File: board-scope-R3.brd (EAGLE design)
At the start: 80 x 55 mm, 71 parts, among them IC3 STM32F103C8T, J2 632723300011, U1 HD3SS3220IRNHT, U2 TUSB8020B, U3 FT600Q-T, U4 ICE40HX1K-VQ100VQ-100, U5 25F32006WSOI, U7 TPS54386, X1 30Mhz, X2 8Mhz

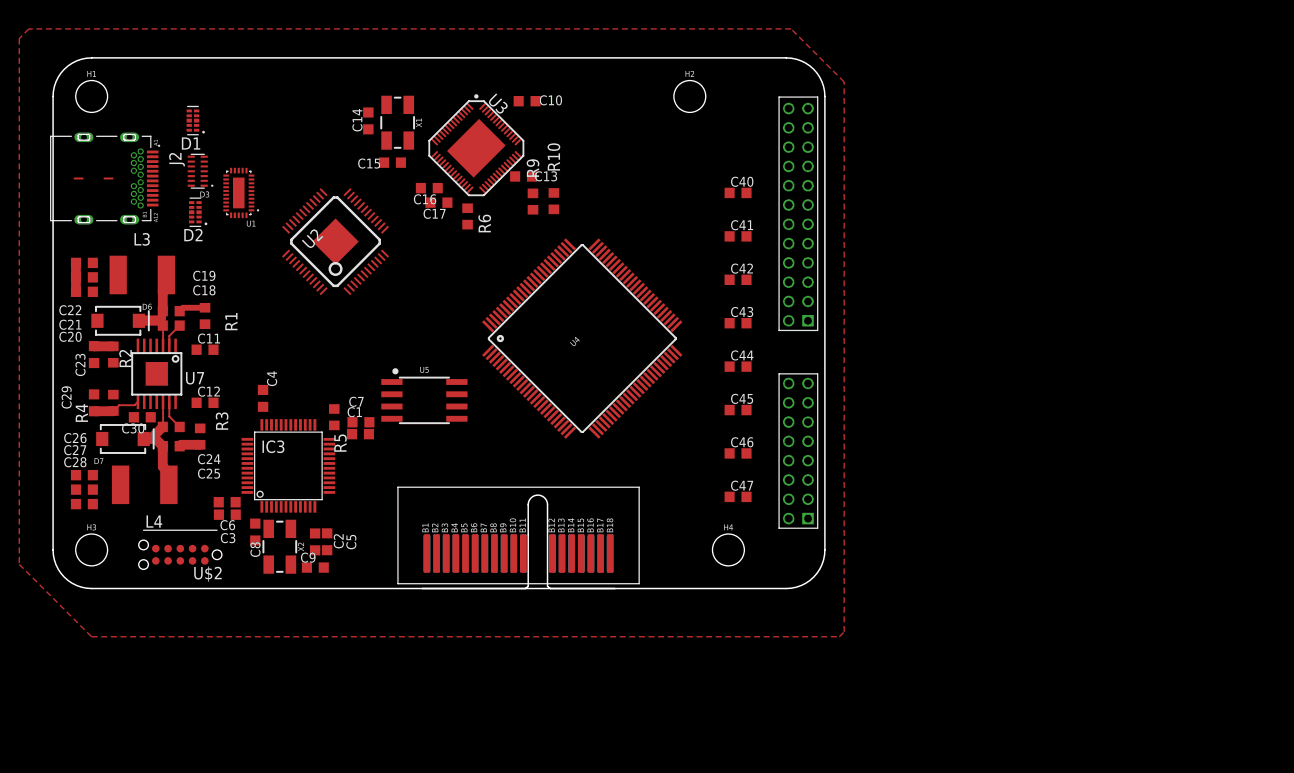
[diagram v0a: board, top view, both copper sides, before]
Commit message: routed power and usb
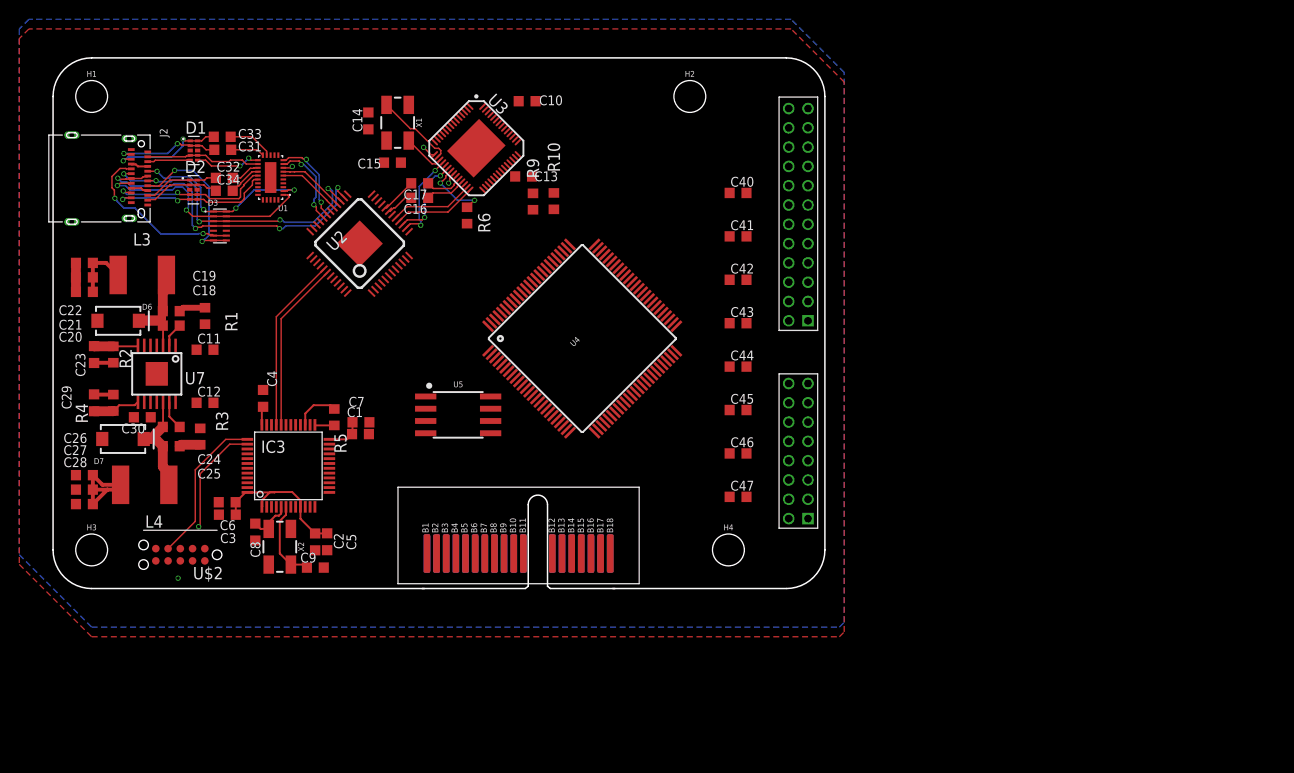
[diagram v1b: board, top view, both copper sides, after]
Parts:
- added C31, C32, C33, C34: 0.47uF, rcl:C0603K
- J2: value 632723300011 -> 12401598E4#2A; device 632723300011:WURTH_632723X00011 -> 12401598E4_2A:AMPHENOL_12401598E4#2A
- moved D3 6.12 mm to (27.3, 47.6), turned to 0 degrees
- moved U5 3.81 mm to (52.0, 28.0)
- moved U1 3.67 mm to (32.5, 52.6)
- moved J2 3.40 mm to (19.1, 52.5)
- moved D1 3.10 mm to (24.6, 55.4), turned to 0 degrees
- moved C17 2.83 mm to (48.0, 52.0)
- moved U2 2.51 mm to (41.8, 45.8)
- moved D2 2.34 mm to (24.6, 51.3), turned to 0 degrees
- moved C16 1.41 mm to (48.0, 50.5)
- moved R6 0.11 mm to (52.9, 48.7)
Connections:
- removed net N$10: J2.S1, J2.S2, J2.S3, J2.S4, J2.S5, J2.S6
- removed net N$11: J2.A1, J2.A12, J2.B1, J2.B12, J2.GND, J2.GND1
- removed net N$12: U1.16
- removed net N$13: U1.17
- removed net N$14: U1.20
- removed net N$15: U1.21
- removed net N$9: J2.A4, J2.A9, J2.B4, J2.B9
- new net SSRXN1_UP_C: C33.2, U1.14
- new net SSRXN2_UP_C: C32.2, U1.18
- new net SSRXP1_UP_C: C31.2, U1.15
- new net SSRXP2_UP_C: C34.2, U1.19
- net GND: now also J2.A1, J2.A12, J2.B1, J2.B12, J2.SH1, J2.SH2, J2.SH3, J2.SH4
- net SSRXN1_UP: now also C33.1, D1.1, D1.10; no longer D1.4, D1.7, U1.14
- net SSRXN2_UP: now also C32.1, D2.1, D2.10; no longer D2.5, D2.6, U1.18
- net SSRXP1_UP: now also C31.1, D1.2, D1.9; no longer D1.5, D1.6, U1.15
- net SSRXP2_UP: now also C34.1, D2.2, D2.9; no longer D2.4, D2.7, U1.19
- net SSTXN1_UP: now also D1.5, D1.6, U1.16; no longer D1.1, D1.10
- net SSTXN2_UP: now also D2.4, D2.7, U1.20; no longer D2.2, D2.9
- net SSTXP1_UP: now also D1.4, D1.7, U1.17; no longer D1.2, D1.9
- net SSTXP2_UP: now also D2.5, D2.6, U1.21; no longer D2.1, D2.10
- net V_USB: now also J2.A4, J2.A9, J2.B4, J2.B9
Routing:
- net DP_UP: track 0.00 -> 34.7 mm, vias 0 -> 4
- net +3V3: track 0.00 -> 34.0 mm, vias 0 -> 3
- net DN_UP: track 0.00 -> 32.2 mm, vias 0 -> 5
- net CC2: track 0.00 -> 23.8 mm, vias 0 -> 2
- net CC1: track 0.00 -> 20.3 mm, vias 0 -> 4
- net BM_DP: track 0.00 -> 18.2 mm
- net SBU2: track 0.00 -> 18.0 mm, vias 0 -> 2
- net BM_TDI: track 0.00 -> 17.9 mm, vias 0 -> 2
- net BM_DM: track 0.00 -> 17.8 mm
- net SSTXN2_UP: track 0.00 -> 16.9 mm, vias 0 -> 2
- net SSTXP2_UP: track 0.00 -> 16.9 mm, vias 0 -> 2
- net SBU1: track 0.00 -> 16.3 mm, vias 0 -> 2
- net BM_TCK: track 0.00 -> 16.0 mm
- net VCCINT: track 0.00 -> 13.5 mm
- net SSTXP1_UP: track 0.00 -> 12.0 mm
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- added copper zone on layer 15, net GND
- added copper zone on layer 16, net GND
- added copper zone on layer 2, net GND
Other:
- outline, holes or cut-outs redrawn

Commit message: saving
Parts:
- removed C44, C45, C46, C47: 0.1uF, rcl:C0603K
- added B10, B11, B12, B13, B14, B15, B8, B9: (no value), SparkFun-LED:LED-0603
- added C600, C610, C620, C650, C651: 1uF, rcl:C0603K
- added C601, C611, C621, C652, C653: 0.1uF, rcl:C0603K
- added C602, C603, C612, C613, C622, C623, C654, C655, C656: 10nF, rcl:C0603K
- added D4: 1A/23V/620mV, SparkFun-DiscreteSemi:SOD-323
- added R11: 330, mylib:CTS743C163
- added R7, R8: 10k, rcl:R0603
- added S1, S3: (no value), mylib:TACTILE_SWITCH_SMD_5.2MM
- C630: value 0.1uF -> 1uF
- C632, C633: value 0.1uF -> 10nF
- U4: value ICE40HX1K-VQ100VQ-100 -> ICE40HX1K-VQ100; device ice40hx1k-vq100:TQFP100 -> mylib:QFP50P1600X1600X120-100N
- moved U5 12.4 mm to (40.9, 33.5)
- moved U4 2.62 mm to (66.3, 38.1), turned to 315 degrees
- moved C2 1.22 mm to (38.4, 14.8)
- moved C5 1.22 mm to (39.6, 14.8)
- moved C9 1.22 mm to (38.4, 12.1)
- moved X2 1.22 mm to (34.7, 14.3)
- moved C8 1.22 mm to (32.2, 15.8)
- renumbered C40 to C630, C41 to C631, C42 to C632, C43 to C633
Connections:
- net VPP_DIRECT_FAST renamed VPP_FAST
- removed net GND$0: U4.5
- removed net GND$1: U4.17
- removed net GND$2: U4.23
- removed net GND$3: U4.32
- removed net GND$4: U4.39
- removed net GND$5: U4.47
- removed net GND$6: U4.55
- removed net GND$8: U4.84
- removed net GND$9: U4.98
- removed net ICE40_VCCIO1: C44.1, C45.1, C46.1, C47.1
- removed net IOT_78: U4.82
- removed net VCC: U4.11, U5.8
- removed net VCCIO_0$1: U4.92
- removed net VCCIO_2: U4.31, U4.38
- removed net VCCIO_3: U4.6
- removed net VCCIO_3$: U4.14
- removed net VCCIO_3$1: U4.22
- removed net VCC_IO_1: U4.58
- removed net VCC_IO_1$1: U4.67
- removed net VDD_SPI_IO: U4.50
- removed net VPP_2V5_PUMP: U4.75
- new net BM_MISO: IC3.40, U4.46, U5.2
- new net BM_MOSI: IC3.41, U4.45, U5.5
- new net BM_SCK: IC3.39, U4.48, U5.6
- new net BTN_A: S1.3
- new net BTN_B: S3.3
- new net ICE_CDONE: IC3.42
- new net ICE_CRESET: IC3.43
- new net ICE_SS: IC3.45, U4.49, U5.1
- new net LED0: R11.9
- new net LED1: R11.10
- new net LED2: R11.11
- new net LED3: R11.12
- new net LED4: R11.13
- new net LED5: R11.14
- new net LED6: R11.15
- new net LED7: R11.16
- new net N$1: D4.C, U4.75
- new net N$13: B8.A, R11.1
- new net N$14: B9.A, R11.2
- new net N$15: B10.A, R11.3
- new net N$2: IC3.46
- new net N$20: B11.A, R11.4
- new net N$21: B12.A, R11.5
- new net N$3: IC3.44, R8.2
- new net N$34: B13.A, R11.6
- new net N$35: B14.A, R11.7
- new net N$36: B15.A, R11.8
- net +3V3: now also D4.A, R7.2, U4.14, U4.22, U4.31, U4.38, U4.50, U4.58, U4.6, U4.67, U4.88, U4.92, U5.8
- net BM_RST: now also R7.1
- net BM_TDO: no longer IC3.39
- net GND: now also B10.C, B11.C, B12.C, B13.C, B14.C, B15.C, B8.C, B9.C, C600.2, C601.2, C602.2, C603.2, C610.2, C611.2, C612.2, C613.2, C620.2, C621.2, C622.2, C623.2, C650.2, C651.2, C652.2, C653.2, C654.2, C655.2, C656.2, R8.1, S1.1, S3.1, U4.17, U4.23, U4.32, U4.39, U4.47, U4.5, U4.55, U4.70, U4.84, U4.98; no longer C44.2, C45.2, C46.2, C47.2, IC3.44
- net ICE40_VCCIO0: now also C600.1, C601.1, C602.1, C603.1, C610.1, C611.1, C612.1, C613.1, C620.1, C621.1, C622.1, C623.1, C650.1, C651.1, C652.1, C653.1, C654.1, C655.1, C656.1
- net VCCINT: now also U4.11, U4.35, U4.61, U4.77
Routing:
- net ICE_SS: track 0.00 -> 55.5 mm, vias 0 -> 2
- net BM_SCK: track 0.00 -> 46.5 mm, vias 0 -> 3
- net BM_MISO: track 0.00 -> 44.2 mm, vias 0 -> 2
- net BM_MOSI: track 0.00 -> 42.3 mm, vias 0 -> 2
- net BM_TMS: track 0.00 -> 19.0 mm, vias 0 -> 2
- net BM_RST: track 0.00 -> 17.5 mm, vias 0 -> 2
- net BM_TDI: track 17.9 -> 5.61 mm, vias 2 -> 0
- net N$3: track 0.00 -> 11.4 mm
- net +3V3: track 34.0 -> 39.3 mm
- net GND: track 3.00 -> 5.94 mm, vias 0 -> 1
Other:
- board text added: "*"
- board text added: "0"
- board text added: "1"
- board text added: "2"
- board text added: "3"
- board text added: "4"
- board text added: "5"
- board text added: "6"
- board text added: "7"

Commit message: saving progress
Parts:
- added B1, B2: (no value), SparkFun-LED:LED-0603
- added C35: 47uF, rcl:C0603K
- added C36, C37: 18pF, rcl:C0603K
- added R12, R18: 900k, rcl:R0603
- added R13, R17: 4.7k, rcl:R0603
- added R14, R15, R16: 200k, rcl:R0603
- added R19, R20: 330, rcl:R0603
- added X3: 24Mhz, SparkFun-Clocks:CRYSTAL-SMD-5X3.2-4PAD
- added Y1: OSCILLATORSMD-5X3, SparkFun-Clocks:OSCILLATOR-SMD-5X3.2
- moved C652 86.3 mm to (53.5, 31.9), turned to 180 degrees
- moved C654 84.3 mm to (53.5, 33.1), turned to 180 degrees
- moved C653 77.1 mm to (56.4, 47.3), turned to 90 degrees
- moved C650 76.2 mm to (57.6, 47.3), turned to 90 degrees
- moved C603 71.1 mm to (51.9, 40.7), turned to 180 degrees
- moved C600 68.9 mm to (59.8, 47.9), turned to 180 degrees
- moved C610 68.3 mm to (52.0, 39.4), turned to 180 degrees
- moved C602 67.5 mm to (52.0, 42.0), turned to 180 degrees
- moved C601 66.8 mm to (55.1, 44.5), turned to 180 degrees
- moved C611 60.4 mm to (53.5, 30.5), turned to 180 degrees
- moved C613 56.7 mm to (61.4, 25.1), turned to 180 degrees
- moved D4 54.1 mm to (79.6, 37.2)
- moved C656 54.1 mm to (79.2, 41.3)
- moved C655 54.1 mm to (79.5, 52.7)
- moved C612 52.5 mm to (61.5, 26.5), turned to 180 degrees
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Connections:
- removed net ICE40_VCCIO0: C600.1, C601.1, C602.1, C603.1, C610.1, C611.1, C612.1, C613.1, C620.1, C621.1, C622.1, C623.1, C630.1, C631.1, C632.1, C633.1, C650.1, C651.1, C652.1, C653.1, C654.1, C655.1, C656.1
- removed net VDD: U2.1
- removed net VDD5: U1.30
- new net ICE_CLK: U4.33, Y1.3
- new net N$10: R15.2, U1.27
- new net N$11: U1.22
- new net N$12: U1.3
- new net N$22: R17.1, U1.29
- new net N$23: R14.2, U1.11
- new net N$24: U1.26
- new net N$37: R16.2, U1.23
- new net N$38: U1.24
- new net N$39: U1.25
- new net N$4: R12.1, U1.5
- new net N$40: U2.3
- new net N$41: U2.22
- new net N$42: U2.36
- new net N$43: U2.21
- new net N$44: U2.35
- new net N$45: R18.2, U2.10
- new net N$46: U2.6
- new net N$47: U2.8
- new net N$48: U2.4
- new net N$49: U2.5
- new net N$50: U2.47
- new net N$51: U2.46
- new net N$52: U2.44
- new net N$53: U2.43
- new net N$54: C36.1, U2.38, X3.1
- new net N$55: C37.1, U2.39, X3.3
- new net N$56: U$1.B15
- new net N$57: B1.C, R19.2
- new net N$58: U$1.B7
- new net N$59: U4.60
- new net N$60: U$1.B14
- new net N$61: B2.C, R20.2
- new net N$70: U4.12
- new net N$9: R13.2, U1.4
- net +3V3: now also B2.A, C600.1, C601.1, C602.1, C603.1, C610.1, C611.1, C612.1, C613.1, C620.1, C621.1, C622.1, C623.1, C630.1, C631.1, C632.1, C633.1, U$1.A1, U$1.B1, U2.13, U2.18, U2.23, U2.25, U2.33, U2.37, U2.40, U2.48, Y1.1, Y1.4
- net BM_LED0: now also B1.A
- net BM_MISO: now also U$1.A13
- net BM_MOSI: now also U$1.A14
- net BM_RST: now also U$1.B13
- net BM_RX: now also U$1.A17, U4.57
- net BM_SCK: now also U$1.A15
- net BM_TCK: now also U$1.B16
- net BM_TMS: now also U$1.B17
- net BM_TRGT_RST: now also U4.54
- net BM_TRGT_TCK: now also U4.51
- net BM_TRGT_TDI: now also U4.56
- net BM_TRGT_TDO: now also U4.53
- net BM_TRGT_TMS: now also U4.52
- net BM_TX: now also U$1.A16, U4.59
- net FT_D0: now also U4.10
- net FT_D1: now also U4.9
- net FT_D2: now also U4.8
- net FT_D3: now also U4.7
- net FT_D4: now also U4.4
- net FT_D5: now also U4.3
- net FT_D6: now also U4.2
- net FT_D7: now also U4.1
- net GND: now also C35.2, C36.2, C37.2, R13.1, R17.2, R18.1, R19.1, R20.1, U$1.A11, U$1.A12, U$1.B11, U$1.B12, U1.12, U1.31, U2.P$1, Y1.2
- net ICE_CDONE: now also U$1.B8, U4.43
- net ICE_CRESET: now also U$1.B9, U4.44
- net ICE_SS: now also U$1.B10
- net N$18: now also U2.2; no longer U1.31
- net VCCINT: now also C650.1, C651.1, C652.1, C653.1, C654.1, C655.1, C656.1, U2.1, U2.12, U2.30, U2.34, U2.45
- net V_USB: now also C35.1, R12.2, R14.1, R15.1, R16.1, U1.30
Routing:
- net BM_TX: track 0.00 -> 54.7 mm, vias 0 -> 2
- net ICE_CDONE: track 0.00 -> 52.9 mm, vias 0 -> 3
- net ICE_CRESET: track 0.00 -> 52.3 mm, vias 0 -> 3
- net BM_RX: track 0.00 -> 48.9 mm, vias 0 -> 2
- net BM_TCK: track 16.0 -> 62.3 mm, vias 0 -> 2
- net BM_TMS: track 19.0 -> 62.4 mm, vias 2 -> 4
- net BM_TRGT_TDO: track 0.00 -> 38.2 mm, vias 0 -> 2
- net BM_TRGT_TDI: track 0.00 -> 37.6 mm, vias 0 -> 2
- net BM_TRGT_RST: track 0.00 -> 35.6 mm, vias 0 -> 2
- net BM_TRGT_TCK: track 0.00 -> 33.0 mm, vias 0 -> 2
- net BM_TRGT_TMS: track 4.71 -> 35.5 mm, vias 0 -> 2
- net BM_MOSI: track 42.3 -> 60.0 mm, vias 2 -> 3
- net BM_SCK: track 46.5 -> 63.1 mm, vias 3 -> 4
- net BM_MISO: track 44.2 -> 60.7 mm, vias 2 -> 3
- net N$9: track 0.00 -> 15.1 mm, vias 0 -> 2
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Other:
- board text added: "3.3V"

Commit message: saving more..
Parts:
- removed S1, S3: (no value), mylib:TACTILE_SWITCH_SMD_5.2MM
- added C38: 1uF, rcl:C0603K
- added R21: 90.9k, rcl:R0603
- added R22, R25, R26: 10k, rcl:R0603
- added R23: 9.09k 1%, rcl:R0603
- added R24: (no value), rcl:R0603
- added S2: (no value), mylib:TACTILE_SWITCH_SMD_5.2MM
- moved B10 57.8 mm to (68.5, 55.2)
- moved B11 57.8 mm to (70.5, 55.2)
- moved B12 57.8 mm to (72.5, 55.2)
- moved B13 57.8 mm to (74.5, 55.2)
- moved B14 57.8 mm to (76.5, 55.2)
- moved B15 57.8 mm to (78.5, 55.2)
- moved B8 57.8 mm to (64.5, 55.2)
- moved B9 57.8 mm to (66.5, 55.2)
- moved R11 57.8 mm to (70.1, 59.5)
- moved C655 30.3 mm to (65.6, 25.8), turned to 270 degrees
- moved C633 24.8 mm to (79.5, 30.6), turned to 0 degrees
- moved C632 11.8 mm to (79.9, 47.1), turned to 0 degrees
- moved R6 3.23 mm to (49.9, 47.4), turned to 0 degrees
- moved C622 2.62 mm to (78.0, 32.1)
- moved C623 2.62 mm to (78.0, 33.4)
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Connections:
- removed net BTN_A: S1.3
- removed net BTN_B: S3.3
- removed net LED0: R11.9
- removed net LED1: R11.10
- removed net LED2: R11.11
- removed net LED3: R11.12
- removed net LED4: R11.13
- removed net LED5: R11.14
- removed net LED6: R11.15
- removed net LED7: R11.16
- removed net N$59: U4.60
- removed net N$70: U4.12
- removed net USB_VBUS: U2.9
- new net CH01: U$3.P$4, U4.60
- new net CH02: U$3.P$6, U4.64
- new net CH03: U$3.P$8, U4.66
- new net CH04: U$3.P$10, U4.69
- new net CH05: U$3.P$12, U4.72
- new net CH06: U$3.P$14, U4.74
- new net CH07: U$3.P$3, U4.63
- new net CH08: U$3.P$5, U4.65
- new net CH09: U$3.P$7, U4.68
- new net CH10: U$3.P$9, U4.71
- new net CH11: U$3.P$11, U4.73
- new net CH12: U$3.P$13, U4.78
- new net CH13: U$4.P$4, U4.79
- new net CH14: U$4.P$6, U4.81
- new net CH15: U$4.P$8, U4.85
- new net CH16: U$4.P$10, U4.87
- new net CH17: U$4.P$12, U4.90
- new net CH18: U$4.P$14, U4.93
- new net CH19: U$4.P$16, U4.95
- new net CH20: U$4.P$18, U4.97
- new net CH21: U$4.P$20, U4.100
- new net CH22: U$4.P$22, U4.41
- new net CH23: U$4.P$3, U4.80
- new net CH24: U$4.P$5, U4.82
- new net CH25: R11.16, U$4.P$7, U4.83
- new net CH26: R11.15, U$4.P$9, U4.86
- new net CH27: R11.14, U$4.P$11, U4.89
- new net CH28: R11.13, U$4.P$13, U4.91
- new net CH29: R11.12, U$4.P$15, U4.94
- new net CH30: R11.11, U$4.P$17, U4.96
- new net CH31: R11.10, U$4.P$19, U4.99
- new net CH32: R11.9, U$4.P$21, U4.1
- new net ICE_RESET: R24.1, S2.3, U4.62
- new net N$62: C38.1, U2.11
- new net N$63: R21.1, R22.2, U2.9
- new net N$64: R23.2, U2.24
- new net N$65: U4.42
- net +3V3: now also R25.2, R26.2, U$3.P$15, U$3.P$16
- net FT_BE0: now also U4.40
- net FT_BE1: now also U4.37
- net FT_CLK: now also U4.13
- net FT_D0: now also U4.25; no longer U4.10
- net FT_D1: now also U4.24; no longer U4.9
- net FT_D10: now also U4.9
- net FT_D11: now also U4.8
- net FT_D12: now also U4.7
- net FT_D13: now also U4.4
- net FT_D14: now also U4.3
- net FT_D15: now also U4.2
- net FT_D2: now also U4.21; no longer U4.8
- net FT_D3: now also U4.20; no longer U4.7
- net FT_D4: now also U4.19; no longer U4.4
- net FT_D5: now also U4.18; no longer U4.3
- net FT_D6: now also U4.16; no longer U4.2
- net FT_D7: now also U4.15; no longer U4.1
- net FT_D8: now also U4.12
- net FT_D9: now also U4.10
- net FT_GPIO_0: now also U4.27
- net FT_GPIO_1: now also U4.26
- net FT_OE: now also U4.28
- net FT_RD: now also U4.29
- net FT_RST: now also R26.1
- net FT_RXF: now also U4.34
- net FT_SIWU: now also R25.1
- net FT_TXE: now also U4.36
- net FT_WR: now also U4.30
- net GND: now also C38.2, R22.1, R23.1, S2.1, U$3.P$1, U$3.P$2, U$4.P$1, U$4.P$2; no longer S1.1, S3.1
- net V_USB: now also R21.2, U$4.P$23, U$4.P$24
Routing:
- net CH25: track 0.00 -> 47.7 mm, vias 0 -> 2
- net CH26: track 0.00 -> 46.0 mm, vias 0 -> 1
- net CH27: track 0.00 -> 45.9 mm, vias 0 -> 1
- net CH22: track 0.00 -> 45.9 mm, vias 0 -> 2
- net CH32: track 0.00 -> 45.7 mm, vias 0 -> 1
- net FT_BE0: track 0.00 -> 45.5 mm, vias 0 -> 2
- net CH28: track 0.00 -> 44.7 mm, vias 0 -> 1
- net FT_BE1: track 0.00 -> 44.5 mm, vias 0 -> 2
- net CH29: track 0.00 -> 43.3 mm, vias 0 -> 1
- net CH30: track 0.00 -> 42.9 mm, vias 0 -> 1
- net CH31: track 0.00 -> 42.9 mm, vias 0 -> 1
- net FT_TXE: track 0.00 -> 41.2 mm, vias 0 -> 2
- net FT_RXF: track 0.00 -> 40.4 mm, vias 0 -> 2
- net FT_WR: track 0.00 -> 36.0 mm, vias 0 -> 2
- net BM_RST: track 17.5 -> 52.8 mm, vias 2 -> 3
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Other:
- board size 80 x 55 mm -> 84 x 55 mm

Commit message: almost done routing
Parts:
- moved H4 4.00 mm to (76.0, 14.0)
- moved R11 2.00 mm to (68.1, 59.5)
- moved C37 1.55 mm to (29.8, 38.2), turned to 270 degrees
- moved S2 1.53 mm to (74.7, 22.2)
- moved R24 1.45 mm to (77.5, 26.3)
- moved R17 0.05 mm to (29.2, 42.1)
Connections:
- net BM_TDI: no longer IC3.38
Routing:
- net GND: track 17.5 -> 395.3 mm, vias 4 -> 134
- net +3V3: track 71.0 -> 389.5 mm, vias 4 -> 30
- net V_USB: track 12.1 -> 182.9 mm, vias 2 -> 6
- net VCCINT: track 23.1 -> 170.7 mm, vias 0 -> 9
- net FT_VUSB_DET: track 1.68 -> 15.7 mm, vias 0 -> 2
- net FT_CLK: track 14.4 -> 22.1 mm
- net FT_DV10: track 19.4 -> 27.1 mm
- net N$62: track 0.00 -> 3.52 mm
- net N$64: track 0.00 -> 2.66 mm
- net N$1: track 0.00 -> 2.60 mm
- net N$19: track 4.63 -> 7.00 mm
- net CH25: track 47.7 -> 49.9 mm
- net N$21: track 3.54 -> 5.78 mm
- net N$35: track 5.69 -> 7.85 mm
- net CH31: track 42.9 -> 44.9 mm
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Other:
- board size 84 x 55 mm -> 80 x 55 mm

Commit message: done routing
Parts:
- R24: value (none) -> 10k
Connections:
- removed net BM_LED0-1: IC3.30
- removed net BM_TDI: U$2.8
- removed net BM_TDO: U$2.6
- removed net FT_WAKE: U3.11
- removed net N$2: IC3.46
- removed net N$56: U$1.B15
- removed net N$58: U$1.B7
- removed net N$6: U$2.7
- removed net N$60: U$1.B14
- removed net N$65: U4.42
- removed net N$8: IC3.19
- removed net VDD33: U2.7
- removed net VUSB_3.0: R9.2
- net +3V3: now also R24.2, U2.7
- net V_USB: now also R9.2
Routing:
- net +3V3: track 389.5 -> 472.5 mm, vias 30 -> 44
- net GND: track 395.3 -> 440.9 mm, vias 134 -> 208
- net VCCINT: track 170.7 -> 204.2 mm, vias 9 -> 11
- net V_USB: track 182.9 -> 198.7 mm, vias 6 -> 9
- net FT_DV10: track 27.1 -> 35.1 mm
- net BM_TDI: track 3.87 -> 0.00 mm, vias 1 -> 0
- net BM_LED0: track 0.00 -> 1.90 mm
- net N$57: track 0.00 -> 1.83 mm
- net N$30: track 10.4 -> 11.6 mm
- net FT_RXF: track 40.4 -> 41.5 mm
- net ICE_SS: track 69.4 -> 70.4 mm
- net BM_RST: track 52.8 -> 53.6 mm
- net BM_MISO: track 60.7 -> 61.5 mm
- net FT_D7: track 19.5 -> 18.6 mm
- net SSTXN1_UP: track 11.5 -> 12.3 mm
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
